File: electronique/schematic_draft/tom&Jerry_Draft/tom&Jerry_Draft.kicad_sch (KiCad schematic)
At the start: 0 parts

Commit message: STM32 KiCAD V2 - 18.09.2024
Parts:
- added D101, D102, D103, D104: LED_ABGR, symbol Device:LED_ABGR
- added IC102: LP5812CDSDR, SON65P300X300X80-9N-D, symbol LP5812CDSDR:LP5812CDSDR
- added IC103: TCA9555RTWR, QFN50P400X400X80-25N-D, symbol TCA9555RTWR:TCA9555RTWR
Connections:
- new net: D101.3 (GK), D102.4 (RK), D103.1 (A), D104.2 (BK), IC102.6 (OUT2)
- new net: D101.4 (RK), D102.1 (A), D103.2 (BK), D104.3 (GK), IC102.7 (OUT1)
- new net: D101.1 (A), D102.2 (BK), D103.3 (GK), D104.4 (RK), IC102.8 (OUT0)
- new net: D101.2 (BK), D102.3 (GK), D103.4 (RK), D104.1 (A), IC102.5 (OUT3)
- new net +5V: IC102.1 (VCC), IC103.21 (VCC)
- new net Capteurs et IMU/IMU_INT1: IC103.17 (P17)
- new net Capteurs et IMU/IMU_INT2: IC103.16 (P16)
- new net Capteurs et IMU/LIDAR_DEV_EN: IC103.15 (P15)
- new net Capteurs et IMU/LIDAR_M_EN: IC103.14 (P14)
- new net Capteurs et IMU/TOF1_GPIO1: IC103.13 (P13)
- new net Capteurs et IMU/TOF1_SDA: IC102.4 (SDA), IC103.20 (SDA)
- new net Capteurs et IMU/TOF1_XSHUT: IC103.6 (P05)
- new net Capteurs et IMU/TOF2_GPIO1: IC103.12 (P12)
- new net Capteurs et IMU/TOF2_XSHUT: IC103.5 (P04)
- new net Capteurs et IMU/TOF3_GPIO1: IC103.11 (P11)
- new net Capteurs et IMU/TOF3_XSHUT: IC103.4 (P03)
- new net Capteurs et IMU/TOF4_GPIO1: IC103.10 (P10)
- new net Capteurs et IMU/TOF4_XSHUT: IC103.3 (P02)
- new net Capteurs et IMU/TOF5_GPIO1: IC103.8 (P07)
- new net Capteurs et IMU/TOF5_XSHUT: IC103.2 (P01)
- new net Capteurs et IMU/TOF6_GPIO1: IC103.7 (P06)
- new net Capteurs et IMU/TOF6_XSHUT: IC103.1 (P00)
- new net Capteurs et IMU/TOF_SCL: IC102.3 (SCL), IC103.19 (SCL)
- new net GND: IC102.2 (SYNC), IC102.9 (GND), IC103.18 (A0), IC103.23 (A1), IC103.24 (A2), IC103.9 (GND)
- new net STM32/EXPANDER_EXTI: IC103.22 (~{INT})
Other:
- added sheet MUSIQUE (musique.kicad_sch)
- sheet Capteurs et IMU ports: added IMU_INT1, IMU_INT2, IMU_SCL, IMU_SDA, LIDAR_DEV_EN, LIDAR_M_EN, LIDAR_PWM, LIDAR_RX, LIDAR_TX, Moustache_1, Moustache_2, Moustache_3, Moustache_4, TOF1_GPIO1, TOF1_SDA, TOF1_XSHUT, TOF2_GPIO1, TOF2_SDA, TOF2_XSHUT, TOF3_GPIO1, TOF3_SDA, TOF3_XSHUT, TOF4_GPIO1, TOF4_SDA, TOF4_XSHUT, TOF5_GPIO1, TOF5_SDA, TOF5_XSHUT, TOF6_GPIO1, TOF6_SDA, TOF6_XSHUT, TOF_SCL; removed none
- sheet Drivers_moteurs ports: added ADC_2, Codeur1_PH1, Codeur1_PH2, Codeur2_PH1, Codeur2_PH2, PWM_MOT1_CH1, PWM_MOT1_CH2, PWM_MOT2_CH1, PWM_MOT2_CH2; removed none
- sheet STM32 ports: added CC1, CC2, DRIVER_1_FWD, DRIVER_1_REV, DRIVER_2_FWD, DRIVER_2_REV, EXPANDER_EXTI, I2C_MAIN_SCL, I2C_MAIN_SDA, IMU_SCL, IMU_SDA, LIDAR_M_CTR, LIDAR_RX, LIDAR_TX, ODOM1_PHASEA, ODOM1_PHASEB, ODOM2_PHASEA, ODOM2_PHASEB; removed none

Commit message: KiCAD V3 - 18.09.2024
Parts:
- removed D101, D102, D103, D104: LED_ABGR, symbol Device:LED_ABGR
- removed IC102: LP5812CDSDR, SON65P300X300X80-9N-D, symbol LP5812CDSDR:LP5812CDSDR
- added R101, R102, R103, R104: R_Small, symbol Device:R_Small
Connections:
- net +5V: now also R101.1, R102.1, R103.1, R104.1
- net Periphériques/IMU_SCL: now also R102.2
- net Periphériques/IMU_SDA: now also R101.2
- net Periphériques/TOF1_SDA renamed Led_Debug/Led_Debug_SDA
- net Led_Debug/Led_Debug_SDA: now also R104.2
- net Periphériques/TOF_SCL renamed Led_Debug/Led_Debug_SCL
- net Led_Debug/Led_Debug_SCL: now also R103.2
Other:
- sheet Capteurs et IMU renamed Periphériques
- sheet Drivers_moteurs renamed Motors&Drivers
- sheet MUSIQUE renamed Musique
- added sheet Led_Debug (Led_Debug.kicad_sch)
- sheet Alimentation ports: added CC1, CC2; removed none
- sheet Musique ports: added DAC_STM+, DAC_STM-, HP+, HP-; removed none
- sheet STM32 ports: added DAC+, DAC-, MOUSTACHE_1, MOUSTACHE_2, MOUSTACHE_3, MOUSTACHE_4; removed none

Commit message: STM32 KiCAD V4 - 20.09.2024
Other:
- sheet Motors&Drivers ports: added Out_CurrMeas1, Out_CurrMeas2; removed ADC_2
- sheet STM32 ports: added ASSERV1_OUT, ASSERV2_OUT; removed none
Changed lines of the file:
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@@
+	(wire
+		(pts
+			(xy 222.25 78.74) (xy 247.65 78.74)
+		)
+		(stroke
+			(width 0)
+			(type default)
+		)
+	)
 	(wire
 		(pts
@@
 		(pts
 			(xy 82.55 107.95) (xy 82.55 148.59)
+		)
+		(stroke
+			(width 0)
+			(type default)
+		)
+	)
+	(wire
+		(pts
+			(xy 222.25 81.28) (xy 247.65 81.28)
 		)
 		(stroke
@@
 	(sheet
 		(at 247.65 43.18)
-		(size 40.64 34.29)
+		(size 40.64 43.18)
 		(fields_autoplaced yes)
 		(stroke
@@
 		)
 		(property "Sheetfile" "MoteurProjet_sch.kicad_sch"
-			(at 247.65 78.0546 0)
+			(at 247.65 86.9446 0)
 			(effects
 				(font
@@
 			)
 		)
-		(pin "ADC_2" input
-			(at 288.29 58.42 0)
-			(effects
-				(font
-					(size 1.27 1.27)
-				)
-				(justify right)
-			)
-		)
 		(pin "PWM_MOT2_CH2" input
 			(at 247.65 59.69 180)
@@
 		(pin "PWM_MOT2_CH1" input
 			(at 247.65 57.15 180)
+			(effects
+				(font
+					(size 1.27 1.27)
+				)
+				(justify left)
+			)
+		)
+		(pin "Out_CurrMeas2" input
+			(at 247.65 81.28 180)
+			(effects
+				(font
+					(size 1.27 1.27)
+				)
+				(justify left)
+			)
+		)
+		(pin "Out_CurrMeas1" input
+			(at 247.65 78.74 180)
 			(effects
 				(font
@@
 			)
 		)
+		(pin "ASSERV1_OUT" input
+			(at 222.25 78.74 0)
+			(effects
+				(font
+					(size 1.27 1.27)
+				)
+				(justify right)
+			)
+		)
+		(pin "ASSERV2_OUT" input
+			(at 222.25 81.28 0)
+			(effects
+				(font
+					(size 1.27 1.27)
+				)
+				(justify right)
+			)
+		)

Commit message: STM32 KiCAD V5 - 20.09.2024
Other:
- sheet Motors&Drivers ports: added Out1_CurrentMeas, Out2_CurrentMeas; removed Out_CurrMeas1, Out_CurrMeas2
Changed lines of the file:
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@@
+	(wire
+		(pts
+			(xy 246.38 138.43) (xy 250.19 138.43)
+		)
+		(stroke
+			(width 0)
+			(type default)
+		)
+	)
 	(wire
 		(pts
@@
 		(pts
 			(xy 130.81 104.14) (xy 130.81 111.76)
+		)
+		(stroke
+			(width 0)
+			(type default)
+		)
+	)
+	(wire
+		(pts
+			(xy 246.38 135.89) (xy 250.19 135.89)
 		)
 		(stroke
@@
 			)
 		)
-		(pin "Out_CurrMeas2" input
+		(pin "Out2_CurrentMeas" input
 			(at 247.65 81.28 180)
 			(effects
@@
 			)
 		)
-		(pin "Out_CurrMeas1" input
+		(pin "Out1_CurrentMeas" input
 			(at 247.65 78.74 180)
 			(effects

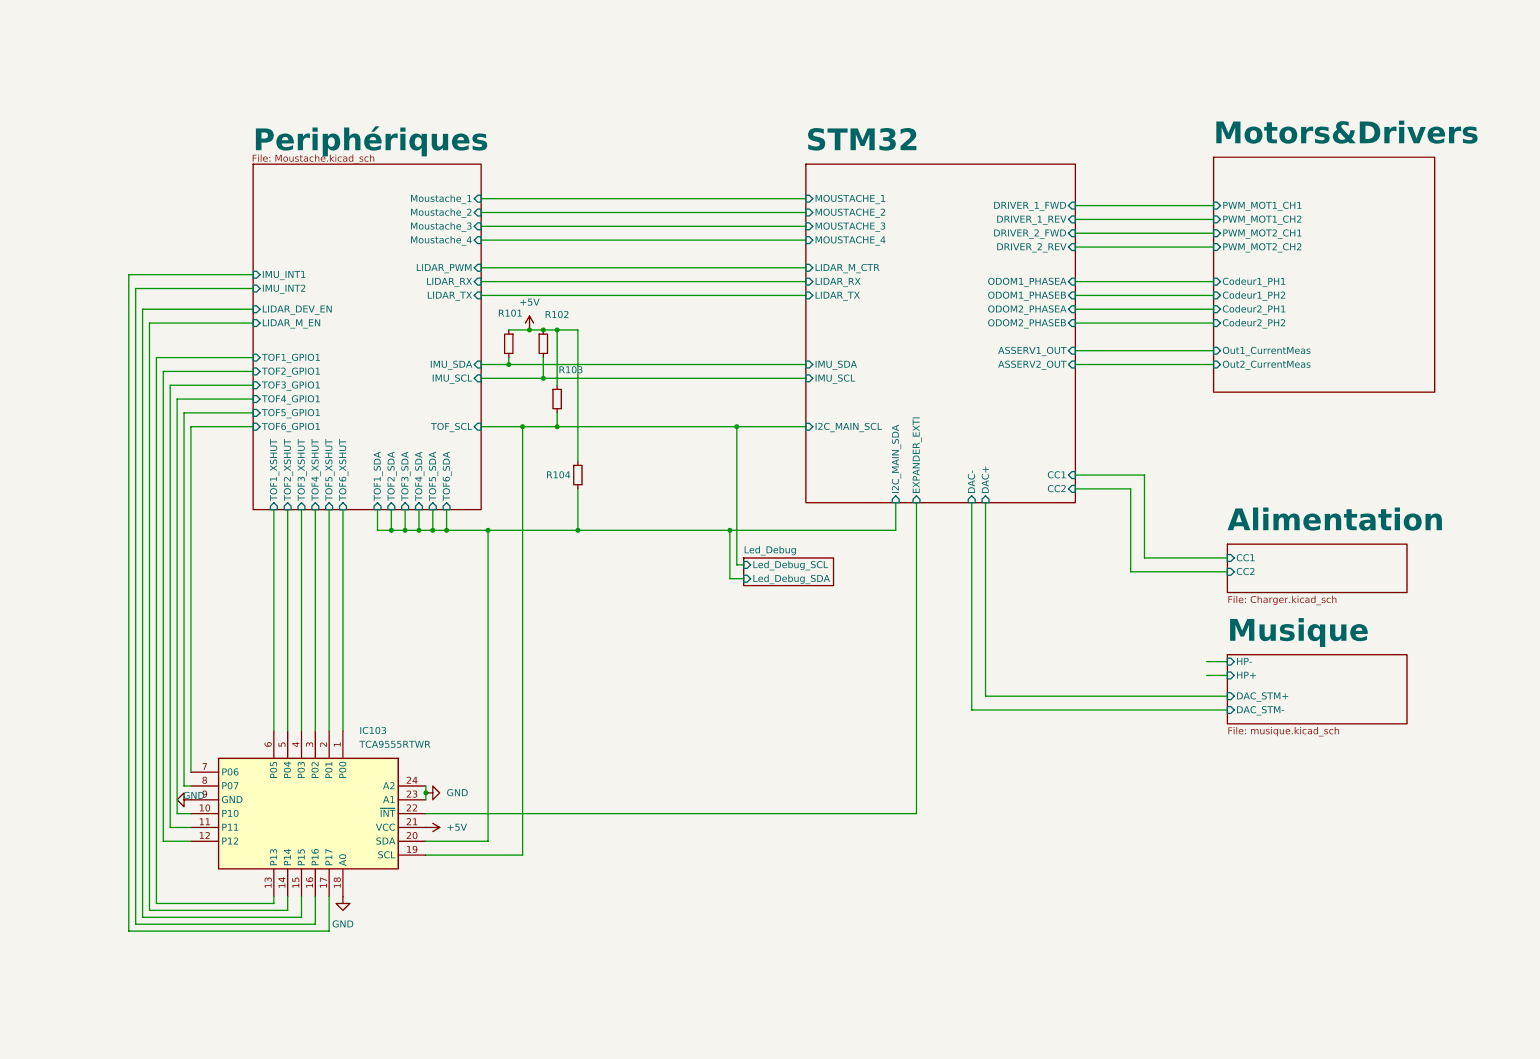
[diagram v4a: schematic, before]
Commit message: STM32 KiCAD V5 - 25.09.2024 - Ajout connecteurs TOF, ...
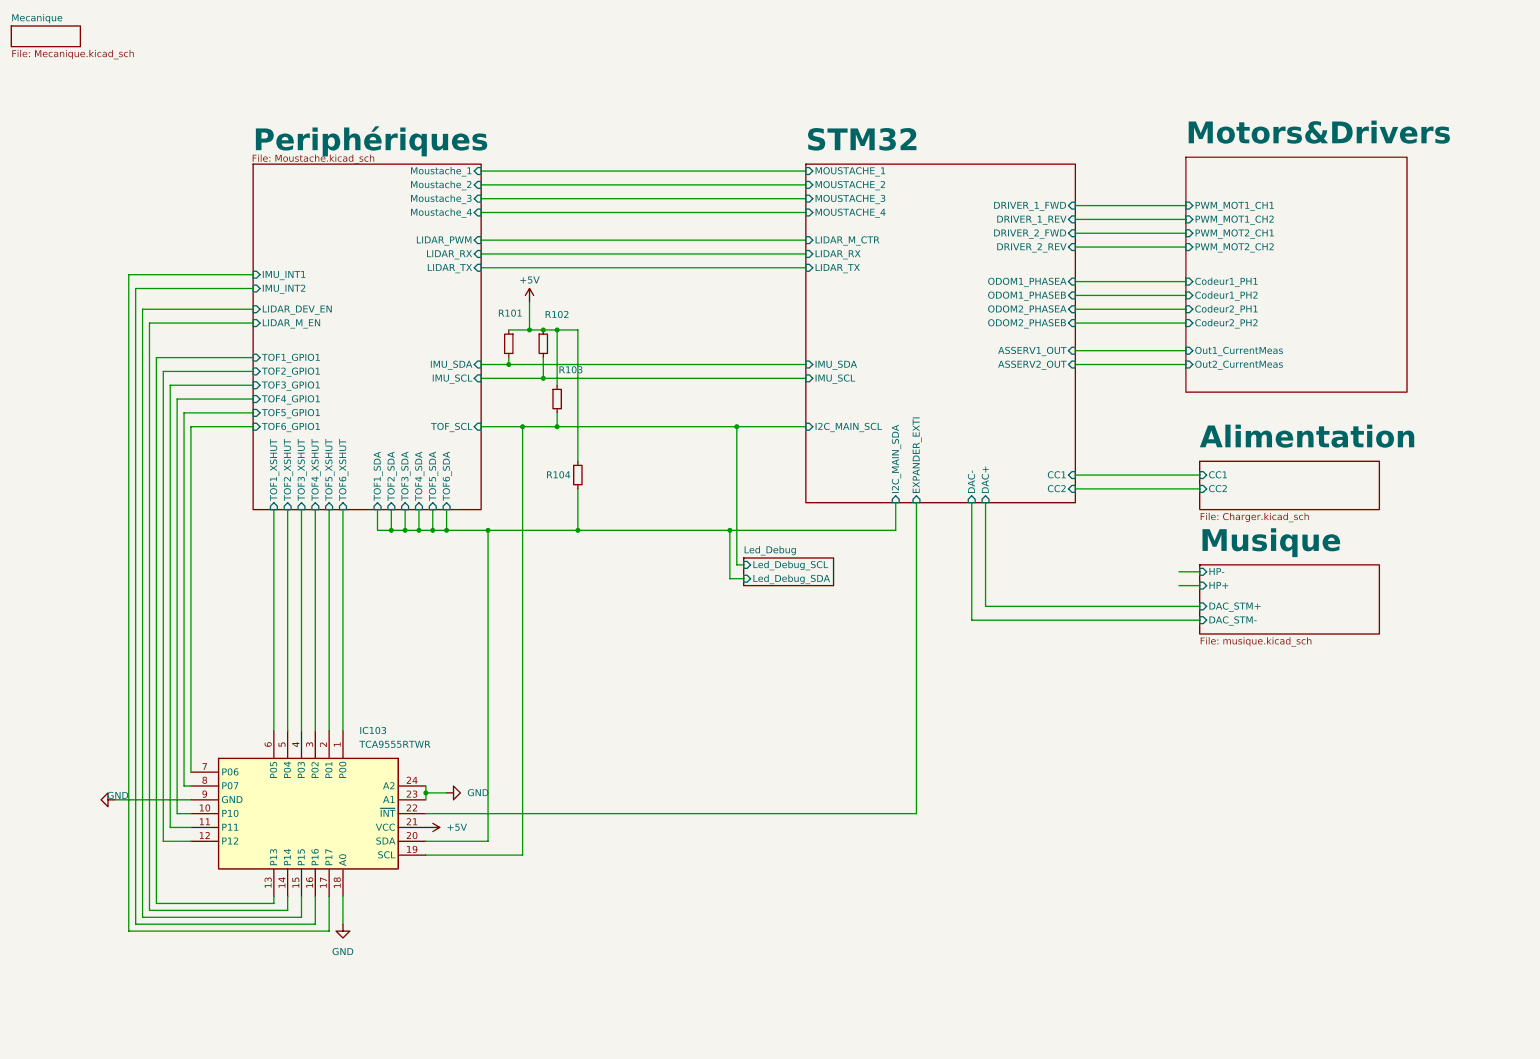
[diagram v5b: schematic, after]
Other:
- added sheet Mecanique (Mecanique.kicad_sch)

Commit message: STM32 KiCAD V6 - 25.09.2024 - Nettoyage des mauvais pins
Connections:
- net Periphériques/LIDAR_DEV_EN is gone; now on net Periphériques/IMU_INT1: IC103.15 (P15)
- net Periphériques/LIDAR_M_EN is gone; now on net Periphériques/IMU_INT2: IC103.14 (P14)
- net Periphériques/IMU_INT1: no longer IC103.17 (P17)
- net Periphériques/IMU_INT2: no longer IC103.16 (P16)
- no-connect marks 0 -> 2
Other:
- sheet Periphériques ports: added none; removed LIDAR_DEV_EN, LIDAR_M_EN, LIDAR_RX
- sheet STM32 ports: added none; removed LIDAR_RX
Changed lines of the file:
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@@
 		(color 0 0 0 0)
 	)
+	(no_connect
+		(at 85.09 179.07)
+	)
+	(no_connect
+		(at 82.55 179.07)
+	)
 	(wire
 		(pts
@@
 	(wire
 		(pts
-			(xy 85.09 185.42) (xy 48.26 185.42)
-		)
-		(stroke
-			(width 0)
-			(type default)
-		)
-	)
-	(wire
-		(pts
 			(xy 118.11 81.28) (xy 172.72 81.28)
 		)
@@
 	(wire
 		(pts
-			(xy 49.53 67.31) (xy 49.53 184.15)
-		)
-		(stroke
-			(width 0)
-			(type default)
-		)
-	)
-	(wire
-		(pts
 			(xy 118.11 80.01) (xy 118.11 81.28)
 		)
@@
 	(wire
 		(pts
-			(xy 49.53 184.15) (xy 82.55 184.15)
-		)
-		(stroke
-			(width 0)
-			(type default)
-		)
-	)
-	(wire
-		(pts
 			(xy 93.98 107.95) (xy 93.98 111.76)
 		)
@@
 	(wire
 		(pts
-			(xy 71.12 67.31) (xy 49.53 67.31)
-		)
-		(stroke
-			(width 0)
-			(type default)
-		)
-	)
-	(wire
-		(pts
 			(xy 130.81 111.76) (xy 158.75 111.76)
 		)
@@
 	(wire
 		(pts
-			(xy 48.26 64.77) (xy 71.12 64.77)
-		)
-		(stroke
-			(width 0)
-			(type default)
-		)
-	)
-	(wire
-		(pts
 			(xy 118.11 74.93) (xy 121.92 74.93)
 		)
@@
 	(wire
 		(pts
-			(xy 82.55 179.07) (xy 82.55 184.15)
-		)
-		(stroke
-			(width 0)
-			(type default)
-		)
-	)
-	(wire
-		(pts
 			(xy 160.02 118.11) (xy 160.02 92.71)
 		)
@@
 	(wire
 		(pts
-			(xy 48.26 185.42) (xy 48.26 64.77)
-		)
-		(stroke
-			(width 0)
-			(type default)
-		)
-	)
-	(wire
-		(pts
 			(xy 58.42 158.75) (xy 59.69 158.75)
 		)
@@
 	(wire
 		(pts
+			(xy 57.15 87.63) (xy 71.12 87.63)
+		)
+		(stroke
+			(width 0)
+			(type default)
+		)
+	)
+	(wire
+		(pts
+			(xy 77.47 181.61) (xy 77.47 179.07)
+		)
+		(stroke
+			(width 0)
+			(type default)
+		)
+	)
+	(wire
+		(pts
+			(xy 80.01 107.95) (xy 80.01 148.59)
+		)
+		(stroke
+			(width 0)
+			(type default)
+		)
+	)
+	(wire
+		(pts
+			(xy 222.25 52.07) (xy 242.57 52.07)
+		)
+		(stroke
+			(width 0)
+			(type default)
+		)
+	)
+	(wire
+		(pts
 			(xy 113.03 60.96) (xy 172.72 60.96)
 		)
@@
 	(wire
 		(pts
-			(xy 57.15 87.63) (xy 71.12 87.63)
-		)
-		(stroke
-			(width 0)
-			(type default)
-		)
-	)
-	(wire
-		(pts
-			(xy 77.47 181.61) (xy 77.47 179.07)
-		)
-		(stroke
-			(width 0)
-			(type default)
-		)
-	)
-	(wire
-		(pts
-			(xy 80.01 107.95) (xy 80.01 148.59)
-		)
-		(stroke
-			(width 0)
-			(type default)
-		)
-	)
-	(wire
-		(pts
-			(xy 222.25 52.07) (xy 242.57 52.07)
-		)
-		(stroke
-			(width 0)
-			(type default)
-		)
-	)
-	(wire
-		(pts
-			(xy 113.03 63.5) (xy 172.72 63.5)
-		)
-		(stroke
-			(width 0)
-			(type default)
-		)
-	)
-	(wire
-		(pts
 			(xy 96.52 107.95) (xy 96.52 111.76)
 		)
@@
 		(pts
 			(xy 55.88 166.37) (xy 59.69 166.37)
-		)
-		(stroke
-			(width 0)
-			(type default)
-		)
-	)
-	(wire
-		(pts
-			(xy 85.09 179.07) (xy 85.09 185.42)
 		)
 		(stroke
@@
 		)
 		(pin "LIDAR_TX" input
-			(at 113.03 63.5 0)
+			(at 113.03 60.96 0)
 			(effects
 				(font
@@
 			)
 		)
-		(pin "LIDAR_RX" input
-			(at 113.03 60.96 0)
-			(effects
-				(font
-					(size 1.27 1.27)
-				)
-				(justify right)
-			)
-		)
 		(pin "Moustache_2" input
 			(at 113.03 48.26 0)
@@
 		)
 		(pin "IMU_INT1" input
-			(at 71.12 64.77 180)
+			(at 71.12 71.12 180)
 			(effects
 				(font
@@
 		)
 		(pin "IMU_INT2" input
-			(at 71.12 67.31 180)
+			(at 71.12 73.66 180)
 			(effects
 				(font
@@
 		(pin "TOF3_XSHUT" input
 			(at 80.01 107.95 270)
-			(effects
-				(font
-					(size 1.27 1.27)
-				)
-				(justify left)
-			)
-		)
-		(pin "LIDAR_M_EN" input
-			(at 71.12 73.66 180)
-			(effects
-				(font
-					(size 1.27 1.27)
-				)
-				(justify left)
-			)
-		)
-		(pin "LIDAR_DEV_EN" input
-			(at 71.12 71.12 180)
 			(effects
 				(font
@@
 		)
 		(pin "LIDAR_TX" input
-			(at 172.72 63.5 180)
-			(effects
-				(font
-					(size 1.27 1.27)
-				)
-				(justify left)
-			)
-		)
-		(pin "LIDAR_RX" input
 			(at 172.72 60.96 180)
 			(effects
